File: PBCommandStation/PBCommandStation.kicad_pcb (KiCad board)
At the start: 2 copper layers, 99.1 x 109.2 mm, 44 parts, among them J201 RJ45, J202 RJ45, P1 POCKETBEAGLE-P1, P2 POCKETBEAGLE-P2, Q101 PN2222A, Q401 TIP120, T201 + 15 in -, T202 + 15 out -, T401 + Power In -, T402 DCC 1, T403 DCC 2, U101 SN75ALS174, U201 TCAN332DR, U202 SN65HVD233-HT, U401 LMD18200, U402 TMP36, U403 LMD18200

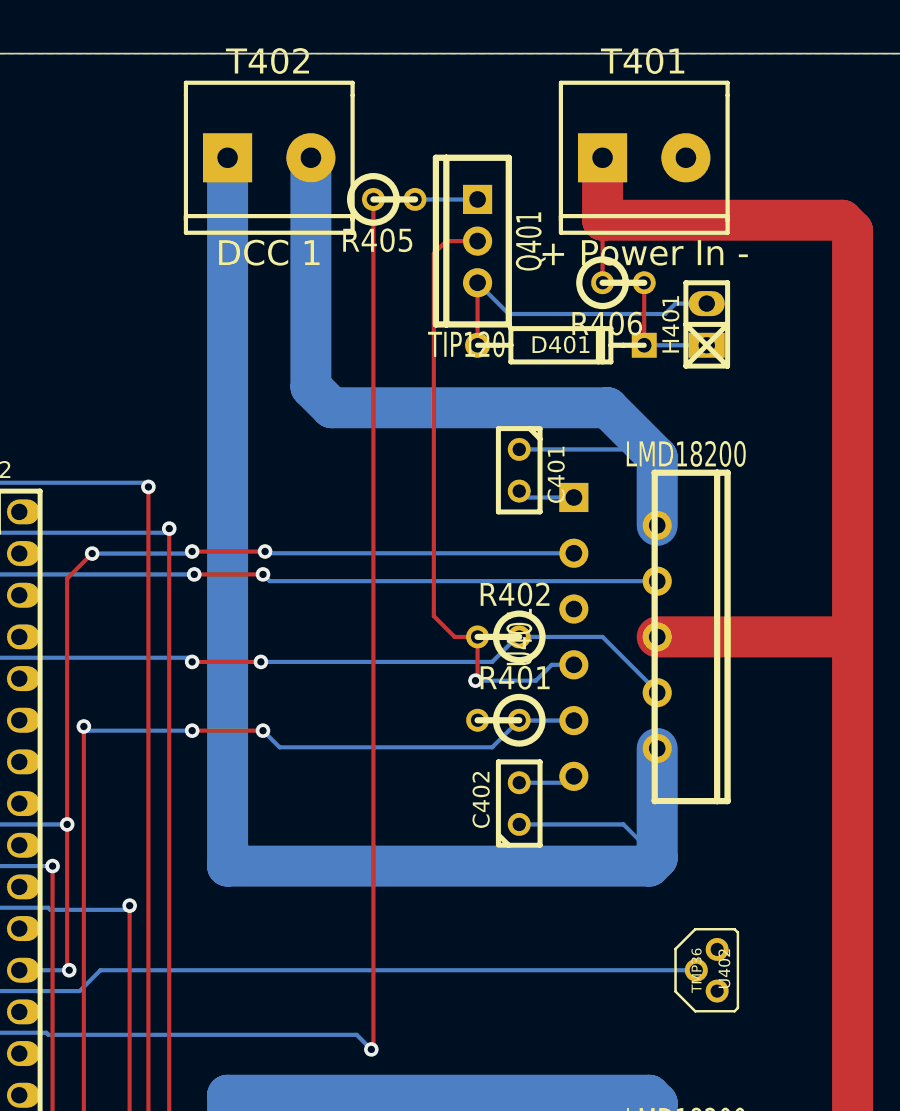
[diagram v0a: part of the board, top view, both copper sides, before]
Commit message: Finished the service mode screen and related dialogs.
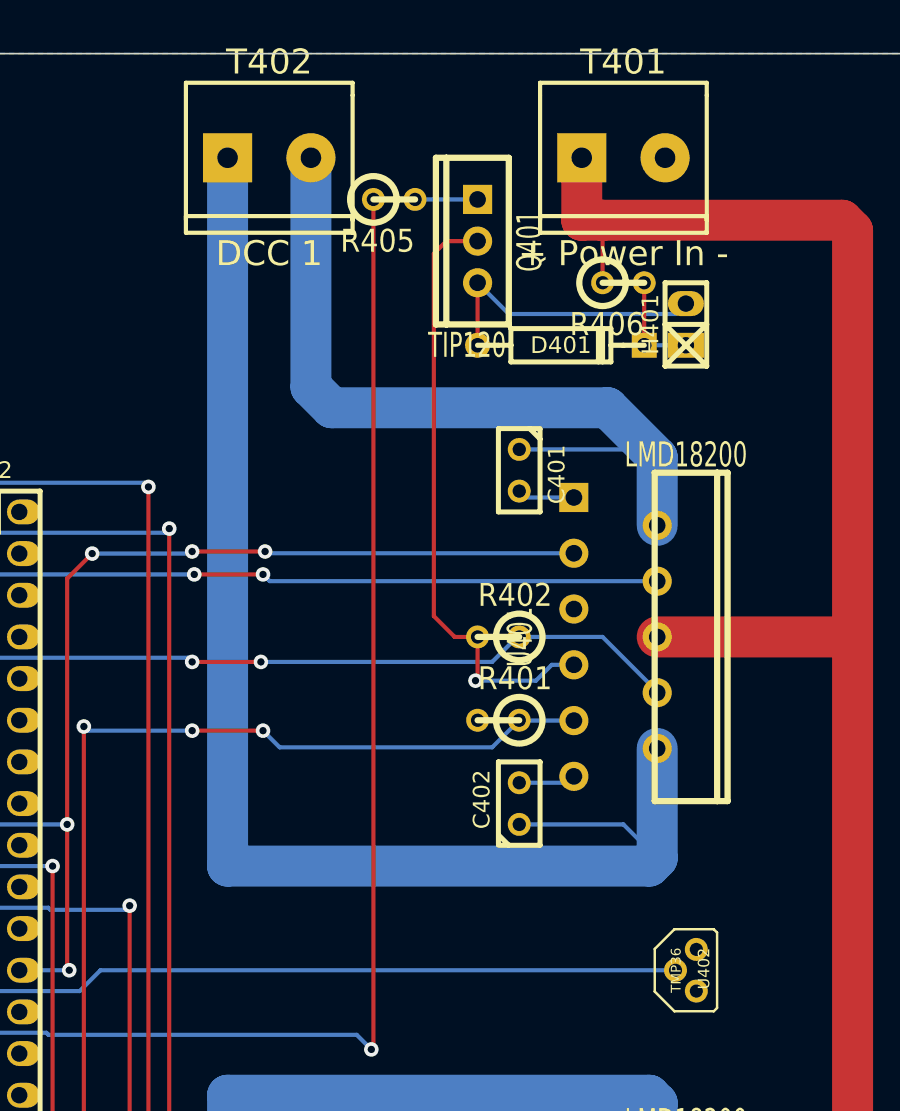
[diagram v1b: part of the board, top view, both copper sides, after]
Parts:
- D401: value 12V -> 1n5349
- R101, R102: value R -> 1K Ohms
- R406: value R -> 33 Ohms 1W
- moved H401 1.27 mm to (195.6, 69.8)
- moved T401 1.27 mm to (191.8, 59.7)
- moved U402 1.27 mm to (195.6, 109.2)
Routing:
- net /Dual Booster/Temp Sense: track 71.4 -> 70.1 mm
- net VCOM: track 112.3 -> 113.6 mm
- net N-0000093: track 18.8 -> 17.6 mm
- net N-0000095: track 7.62 -> 6.35 mm

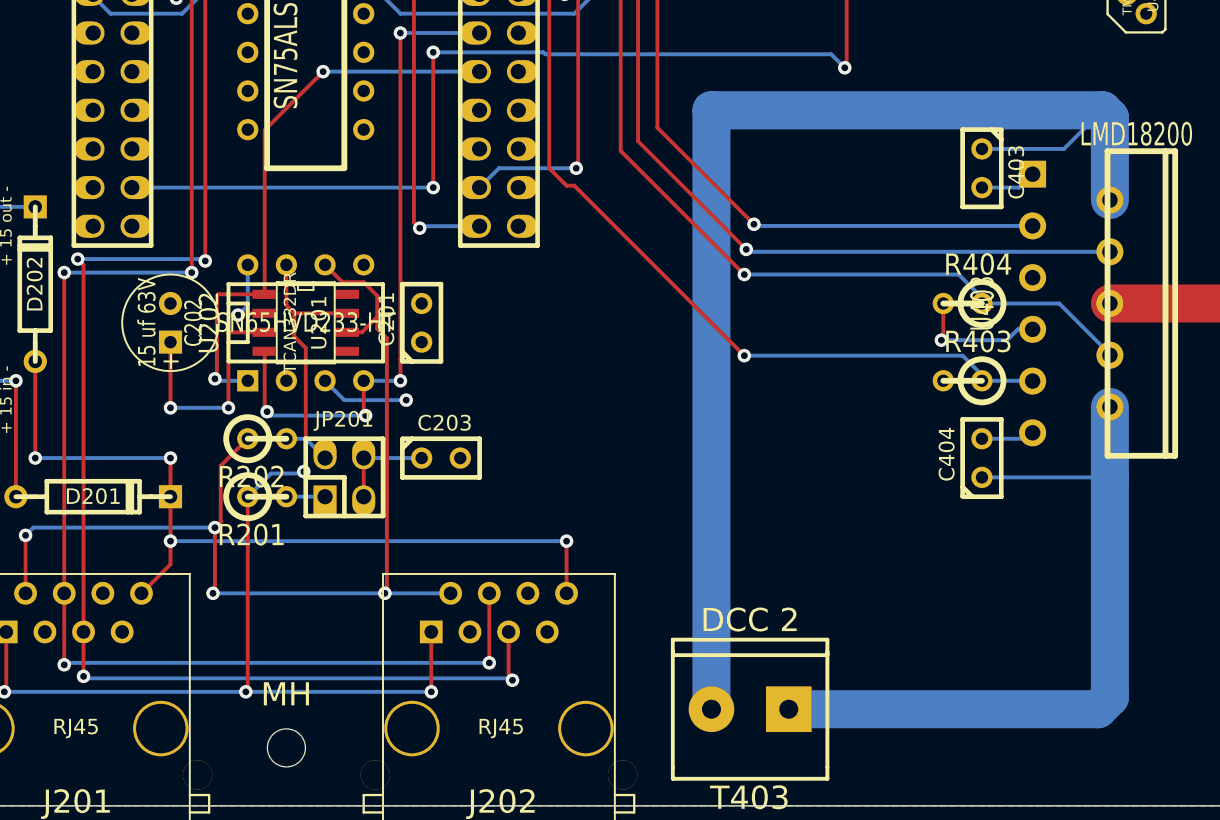
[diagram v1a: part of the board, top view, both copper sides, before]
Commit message: Add Prog Ack Detect circuit.
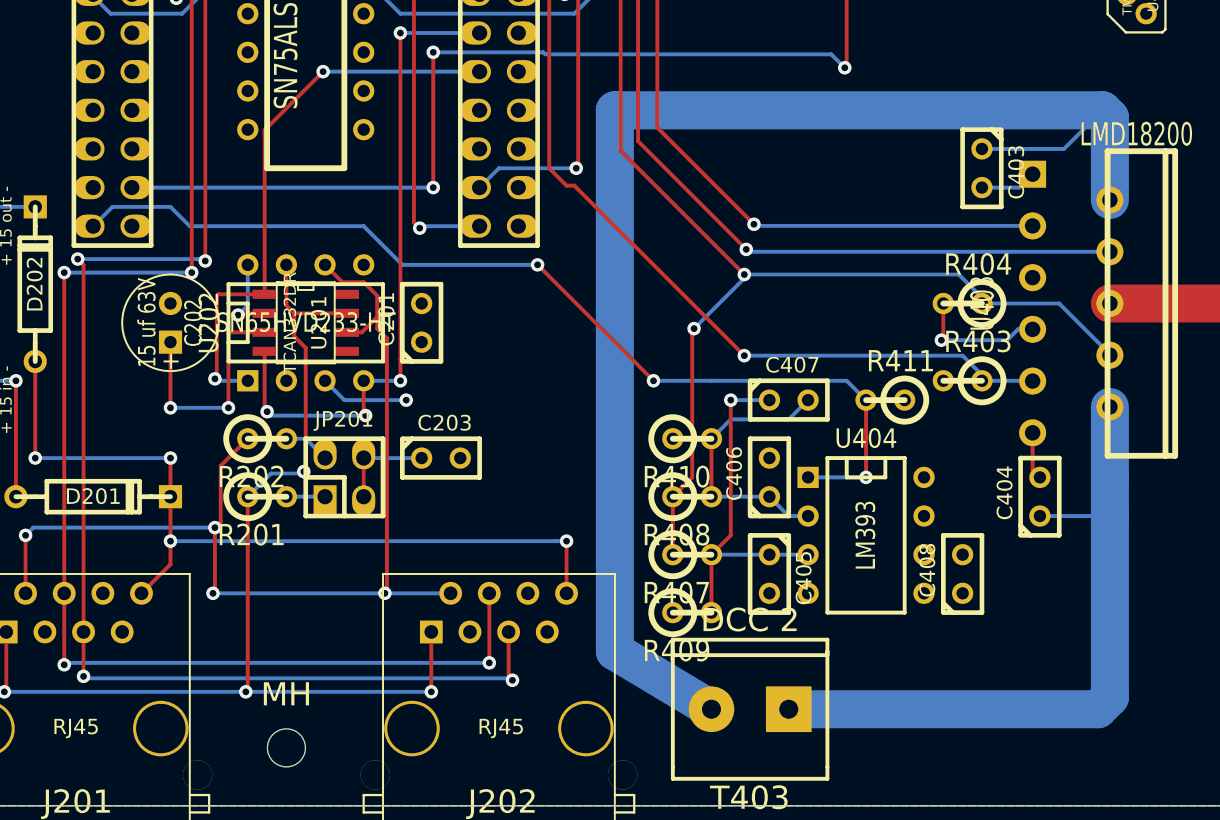
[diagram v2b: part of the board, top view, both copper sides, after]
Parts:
- added C405: 10 nf, C1, F.Cu at (171.4, 147.3)
- added C406: 1 uf, C1, F.Cu at (171.4, 141.0)
- added C407: 10 nf, C1, F.Cu at (172.7, 135.9)
- added C408: 1000 nf, C1, F.Cu at (184.2, 147.3)
- added R407: 10K Ohms, R1, F.Cu at (166.4, 146.1)
- added R408: 13K Ohms, R1, F.Cu at (166.4, 142.2)
- added R409: 1M Ohms, R1, F.Cu at (166.4, 149.9)
- added R410: 1M Ohms, R1, F.Cu at (166.4, 138.4)
- added R411: 10K Ohms, R1, F.Cu at (179.1, 135.9)
- added U404: LM393, DIP-8__300, F.Cu at (177.8, 144.8)
- moved C404 4.58 mm to (189.2, 142.2)
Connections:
- P1 pad 35: (no net) -> /Dual Booster/Ack Detect
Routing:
- net /Dual Booster/Ack Detect: track 0.00 -> 65.5 mm, vias 0 -> 3
- net N-0000096: track 0.00 -> 23.4 mm, vias 0 -> 1
- net /Dual Booster/Current Sense 2: track 88.6 -> 109.0 mm, vias 2 -> 3
- net N-00000101: track 0.00 -> 18.1 mm
- net N-00000106: track 80.2 -> 90.1 mm
- net N-00000108: track 49.9 -> 47.7 mm
